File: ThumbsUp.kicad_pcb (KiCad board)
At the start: 2 copper layers, 280.6 x 468.6 mm, 159 parts, among them J19 52559-1233, J32 Battery, SW2 SW_DIP_x01, U1 ProMicro

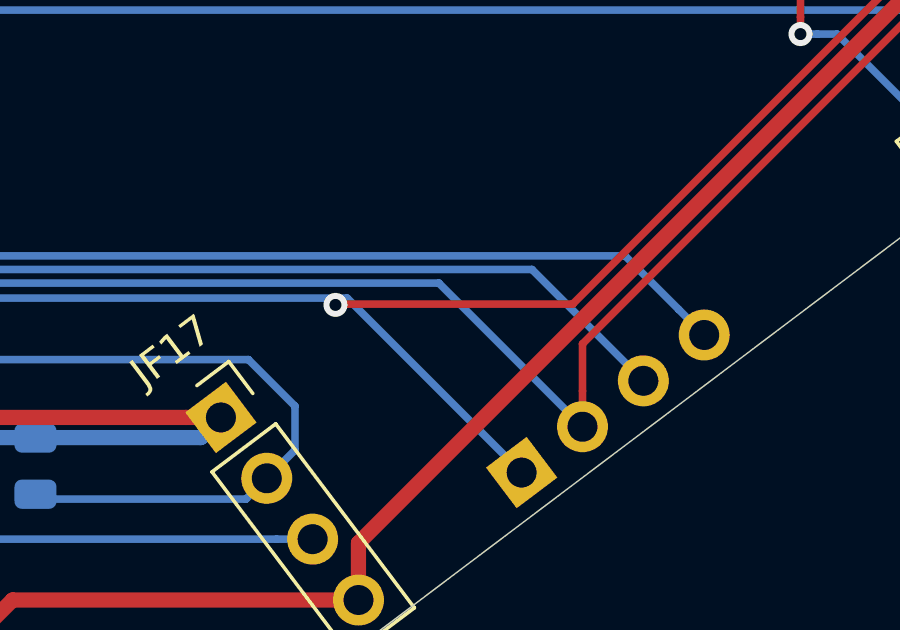
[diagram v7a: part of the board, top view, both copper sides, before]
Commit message: Fixed a missed connection.
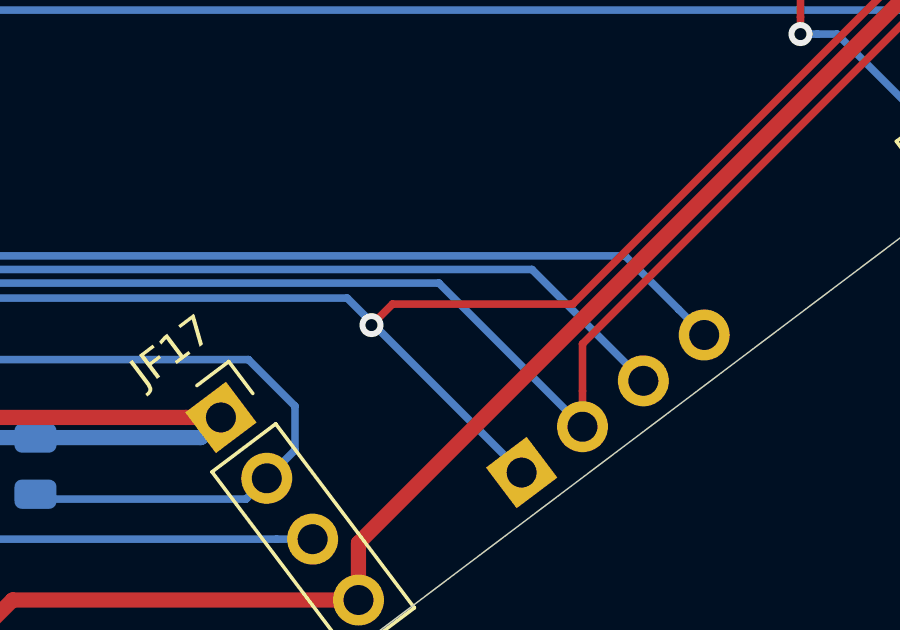
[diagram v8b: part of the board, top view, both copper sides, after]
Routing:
- net COL3: track 337.2 -> 336.2 mm
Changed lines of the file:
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@@
   (segment (start 70.750001 41.750001) (end 71.15 42.15) (width 0.254) (layer F.Cu) (net 42))
   (segment (start 71.15 42.15) (end 71.11 42.19) (width 0.254) (layer B.Cu) (net 42))
-  (via (at 192.9 61.227) (size 0.8) (drill 0.4) (layers F.Cu B.Cu) (net 42))
-  (segment (start 200.807932 61.2) (end 192.9 61.2) (width 0.254) (layer F.Cu) (net 42))
-  (segment (start 228.346107 33.661825) (end 200.807932 61.2) (width 0.254) (layer F.Cu) (net 42))
-  (segment (start 228.346107 31.059804) (end 228.346107 33.661825) (width 0.254) (layer F.Cu) (net 42))
-  (segment (start 192.9 61.2) (end 192.9 61.227) (width 0.254) (layer F.Cu) (net 42))
+  (via (at 194.1 61.9) (size 0.8) (drill 0.4) (layers F.Cu B.Cu) (net 42))
   (segment (start 138.477007 61.198391) (end 137.911322 61.198391) (width 0.254) (layer B.Cu) (net 42))
   (segment (start 138.675398 61) (end 138.477007 61.198391) (width 0.254) (layer B.Cu) (net 42))
   (segment (start 199.105676 66.815353) (end 193.290323 61) (width 0.254) (layer B.Cu) (net 42))
   (segment (start 193.290323 61) (end 138.675398 61) (width 0.254) (layer B.Cu) (net 42))
+  (segment (start 194.8 61.2) (end 194.1 61.9) (width 0.254) (layer F.Cu) (net 42))
+  (segment (start 200.807932 61.2) (end 194.8 61.2) (width 0.254) (layer F.Cu) (net 42))
+  (segment (start 228.346107 31.059804) (end 228.346107 33.661825) (width 0.254) (layer F.Cu) (net 42))
+  (segment (start 228.346107 33.661825) (end 200.807932 61.2) (width 0.254) (layer F.Cu) (net 42))
   (segment (start 48.983641 26.579412) (end 48.983641 25.131244) (width 0.254) (layer B.Cu) (net 43))
   (segment (start 48.983641 30.016359) (end 48.983641 26.579412) (width 0.254) (layer B.Cu) (net 43))
@@
   (segment (start 131.093033 60.743035) (end 131.400001 61.050003) (width 0.254) (layer F.Cu) (net 44))
   (segment (start 131.09198 41.976116) (end 131.093033 41.977169) (width 0.254) (layer F.Cu) (net 44))
+  (segment (start 95.944722 65.094722) (end 95.944722 64.961851) (width 0.254) (layer B.Cu) (net 44))
+  (segment (start 97.05 66.2) (end 95.944722 65.094722) (width 0.254) (layer B.Cu) (net 44))
+  (segment (start 97.05 67.7) (end 97.05 66.2) (width 0.254) (layer B.Cu) (net 44))
+  (segment (start 93.35 71.4) (end 97.05 67.7) (width 0.254) (layer B.Cu) (net 44))
+  (segment (start 91.358892 71.047454) (end 91.711438 71.4) (width 0.254) (layer B.Cu) (net 44))
+  (segment (start 91.711438 71.4) (end 93.35 71.4) (width 0.254) (layer B.Cu) (net 44))
+  (segment (start 99.456571 61.450002) (end 95.944722 64.961851) (width 0.254) (layer B.Cu) (net 44))
+  (segment (start 131.8 61.450002) (end 99.456571 61.450002) (width 0.254) (layer B.Cu) (net 44))
   (via (at 105.84717 -13.95806) (size 0.8) (drill 0.4) (layers F.Cu B.Cu) (net 45))
   (segment (start 105.281485 -13.95806) (end 105.84717 -13.95806) (width 0.254) (layer F.Cu) (net 45))
@@
   (segment (start 131.572999 59.772999) (end 131.700001 59.900001) (width 0.254) (layer F.Cu) (net 45))
   (segment (start 112 18.225142) (end 111.329632 17.554774) (width 0.254) (layer F.Cu) (net 46))
-  (segment (start 95.944722 65.094722) (end 95.944722 64.961851) (width 0.254) (layer B.Cu) (net 44))
-  (segment (start 97.05 66.2) (end 95.944722 65.094722) (width 0.254) (layer B.Cu) (net 44))
-  (segment (start 97.05 67.7) (end 97.05 66.2) (width 0.254) (layer B.Cu) (net 44))
-  (segment (start 93.35 71.4) (end 97.05 67.7) (width 0.254) (layer B.Cu) (net 44))
-  (segment (start 91.358892 71.047454) (end 91.711438 71.4) (width 0.254) (layer B.Cu) (net 44))
-  (segment (start 91.711438 71.4) (end 93.35 71.4) (width 0.254) (layer B.Cu) (net 44))
-  (segment (start 99.456571 61.450002) (end 95.944722 64.961851) (width 0.254) (layer B.Cu) (net 44))
-  (segment (start 131.8 61.450002) (end 99.456571 61.450002) (width 0.254) (layer B.Cu) (net 44))
   (segment (start 168.75 -25.157131) (end 165.545589 -28.361542) (width 0.254) (layer B.Cu) (net 46))
   (segment (start 168.75 -21.75) (end 168.75 -25.157131) (width 0.254) (layer B.Cu) (net 46))
